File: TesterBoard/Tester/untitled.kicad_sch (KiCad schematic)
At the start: 37 parts, among them SW10 SW_Push, SW2 SW_Push, SW3 SW_Push, SW4 SW_Push, SW5 SW_Push, SW6 SW_Push, SW7 SW_Push, SW8 SW_Push, U10 74HC244, U3 74LS14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

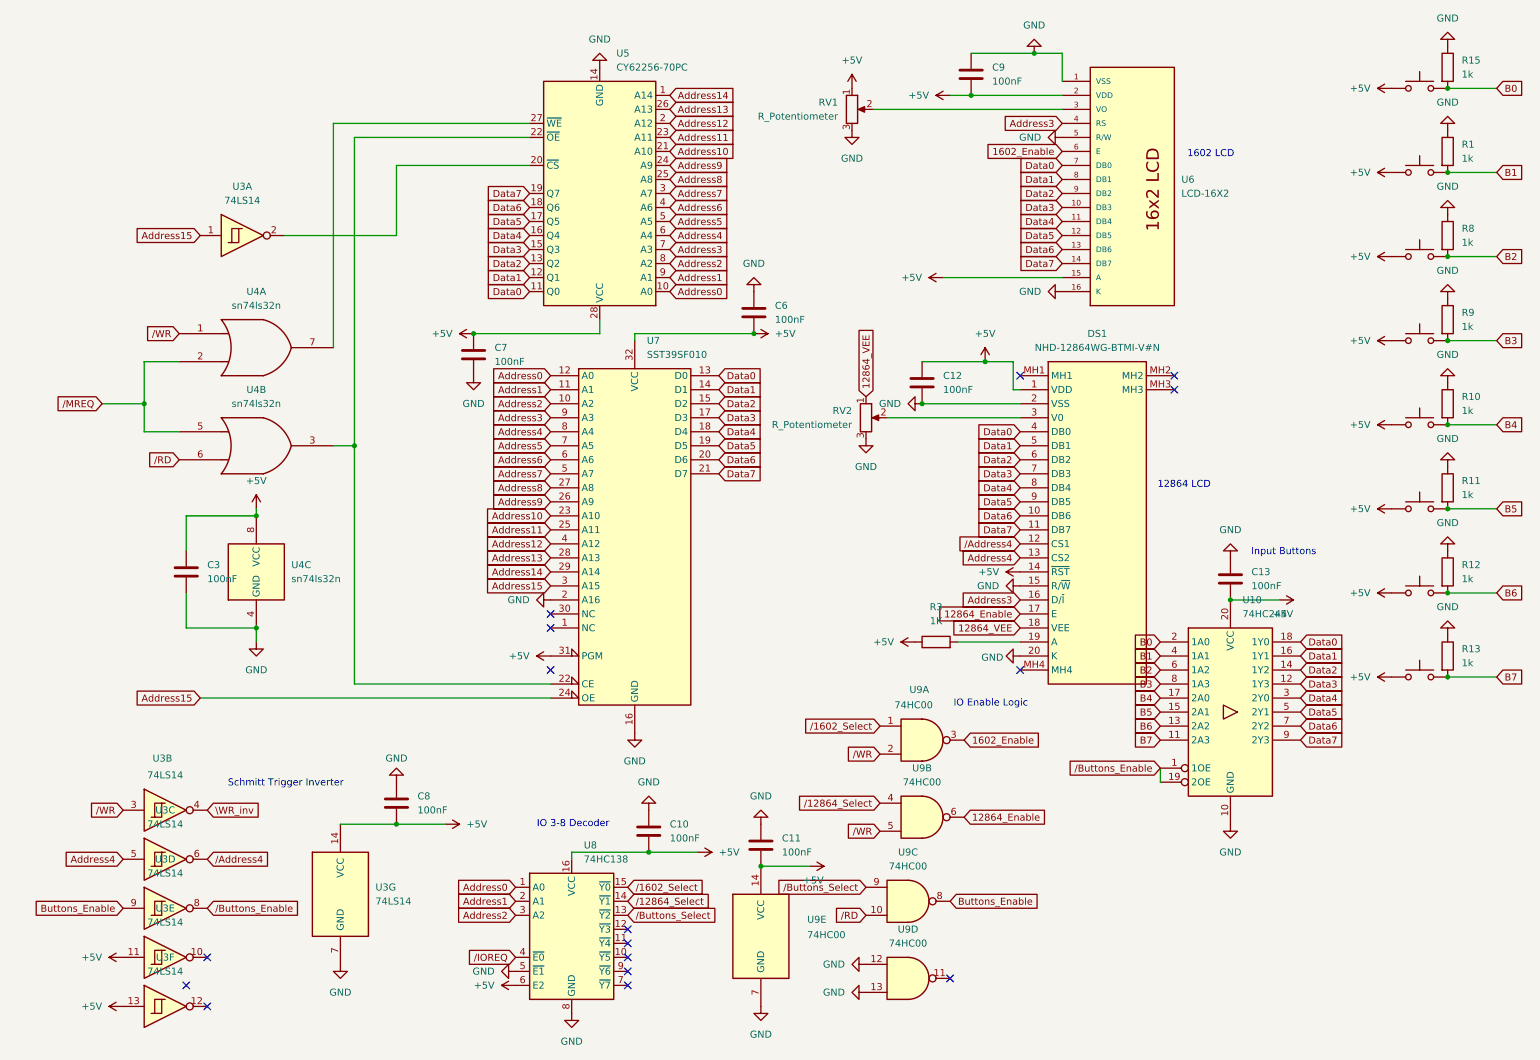
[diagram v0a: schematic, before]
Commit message: updated PCB to fix logic, ready to place and route
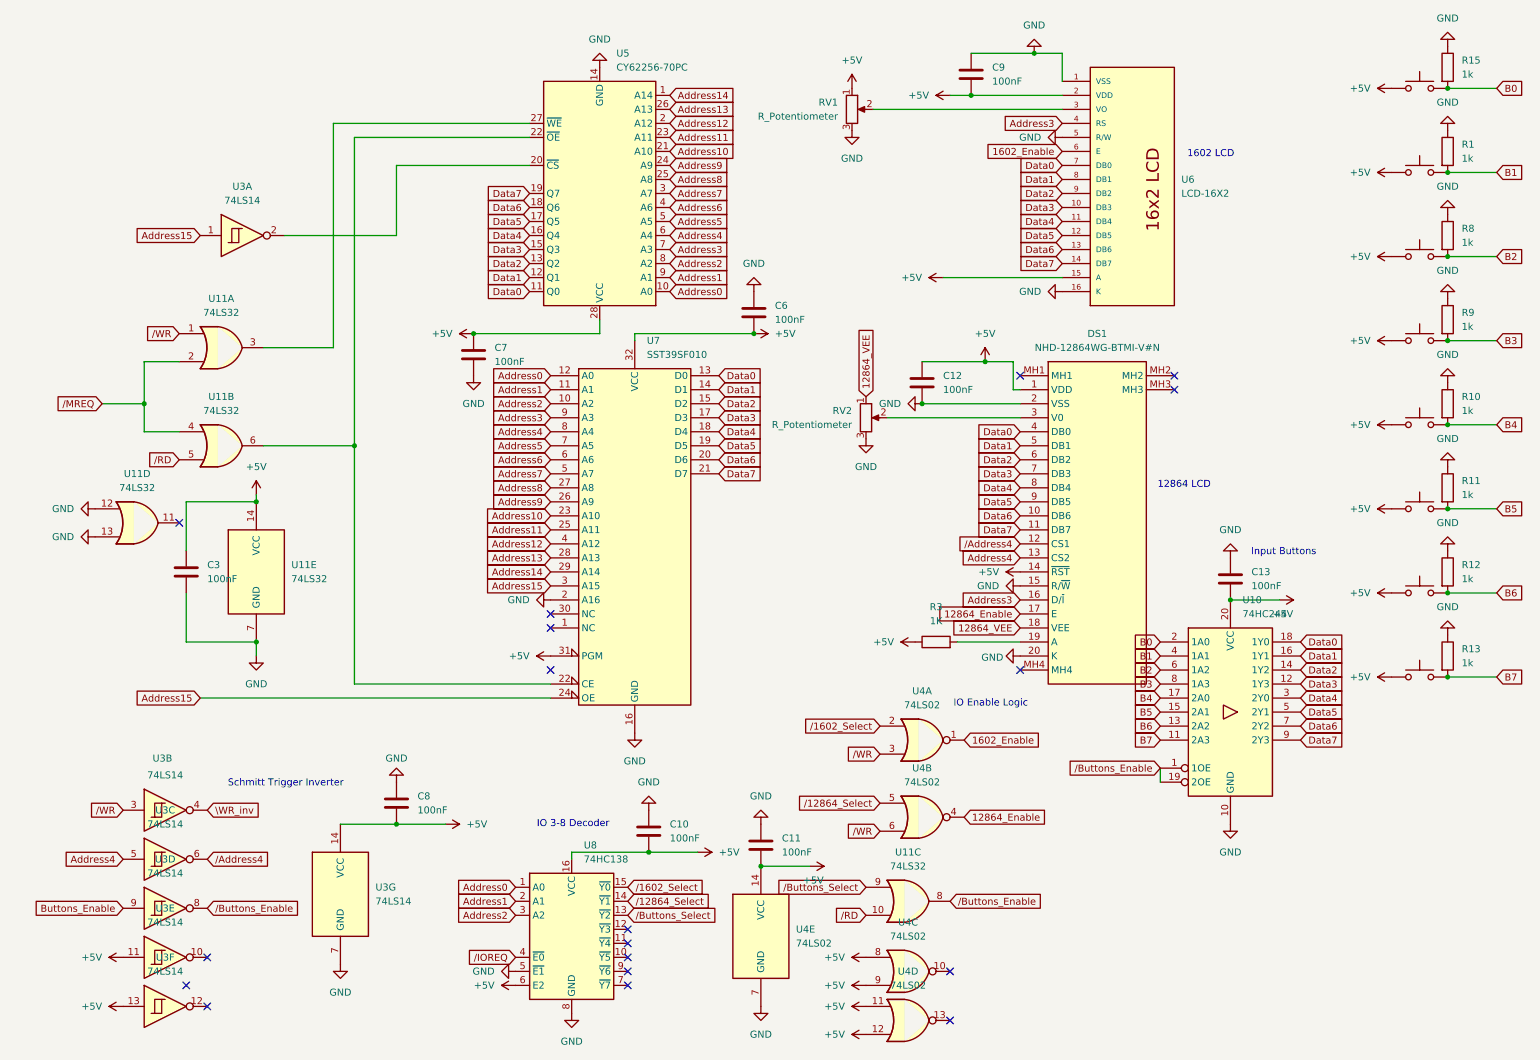
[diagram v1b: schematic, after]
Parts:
- removed U4: sn74ls32n, Package_DIP:DIP-14_W7.62mm_Socket, symbol 74xGxx:74AUC2G32
- removed U9: 74HC00, Package_DIP:DIP-14_W7.62mm_Socket, symbol 74xx:74HC00
- added U11: 74LS32, Package_DIP:DIP-14_W7.62mm_Socket, symbol 74xx:74LS32
- added U4: 74LS02, Package_DIP:DIP-14_W7.62mm_Socket, symbol 74xx:74LS02
- U5: footprint Package_DIP:DIP-28_W15.24mm -> Package_DIP:DIP-28_W15.24mm_Socket
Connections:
- net +5V: now also U11.14 (VCC), U4.11, U4.12, U4.14 (VCC), U4.8, U4.9
- net 12864_Enable: now also U4.4
- net 1602_Enable: now also U4.1
- net GND: now also U11.12, U11.13, U11.7 (GND), U4.7 (GND)
- net /12864_Select: now also U4.5
- net /1602_Select: now also U4.2
- net /Buttons_Enable: now also U11.8
- net /Buttons_Select: now also U11.9
- net /MREQ: now also U11.2, U11.4
- net /RD: now also U11.10, U11.5
- net /WR: now also U11.1, U4.3, U4.6
- net at U5.22 (~{OE}), U7.22 (CE): now also U11.6
- net at U5.27 (~{WE}): now also U11.3
- no-connect marks 16 -> 18

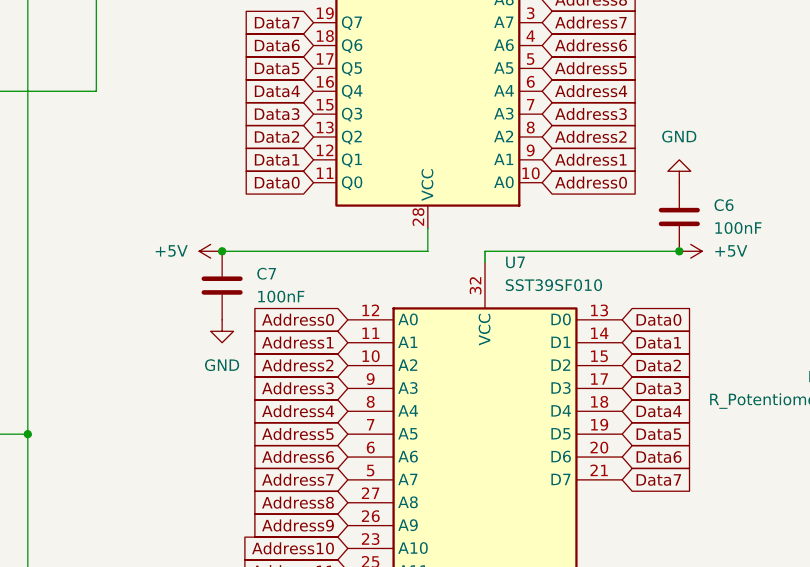
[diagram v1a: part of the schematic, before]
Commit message: minor changes to pcb : labels for schematic
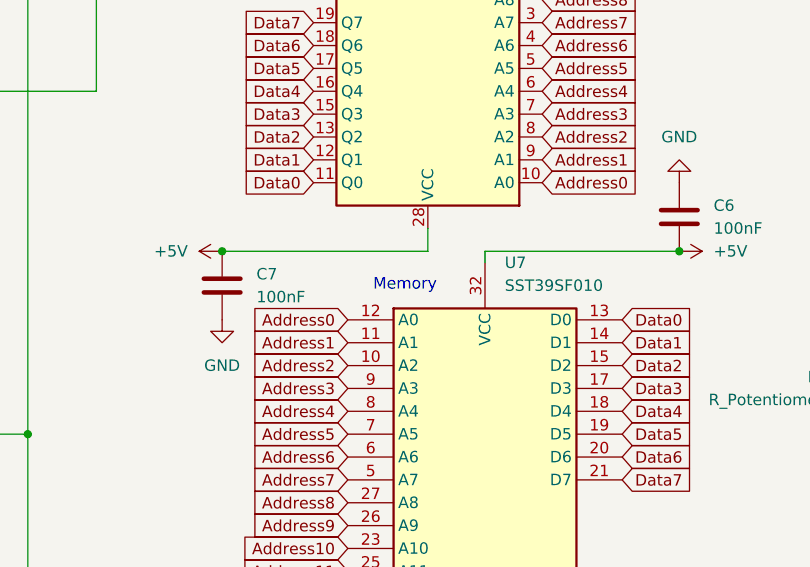
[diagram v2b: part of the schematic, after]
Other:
- note added: "Memory"
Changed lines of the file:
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@@
+		)
+	)
+	(text "Memory"
+		(exclude_from_sim no)
+		(at 109.22 72.39 0)
+		(effects
+			(font
+				(size 1.27 1.27)
+			)
 		)
 	)

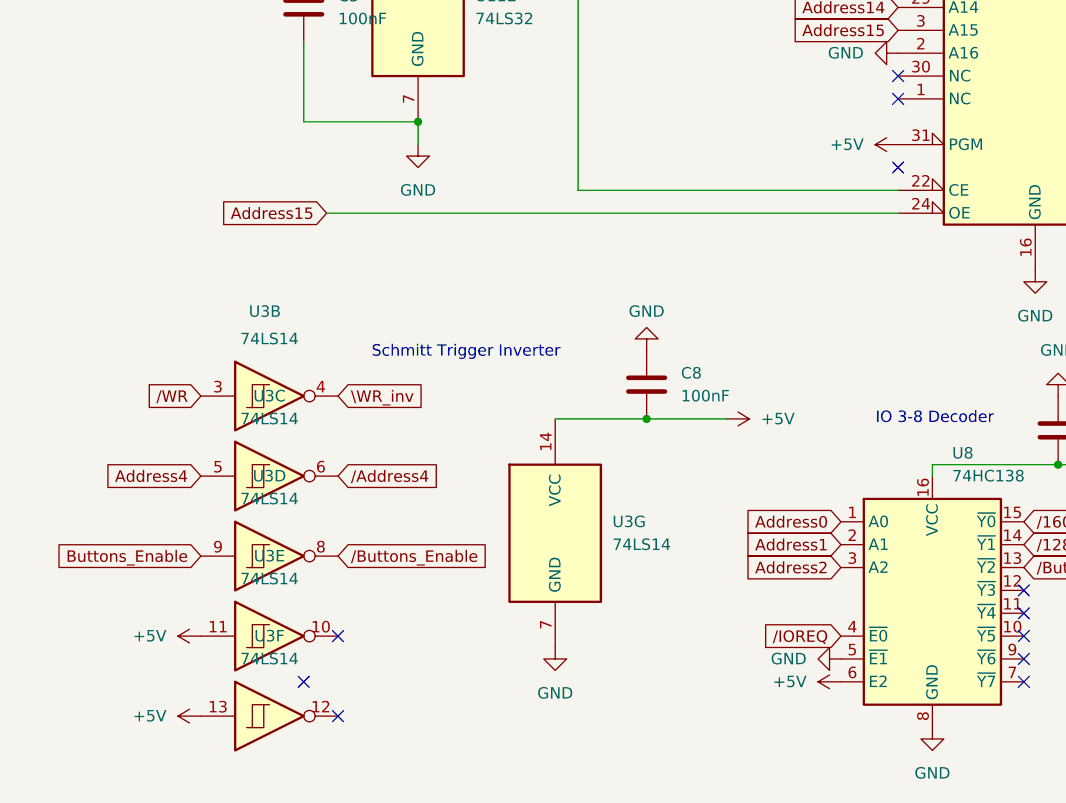
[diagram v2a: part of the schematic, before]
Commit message: Cleared errors on schematic - superfluous enable signal
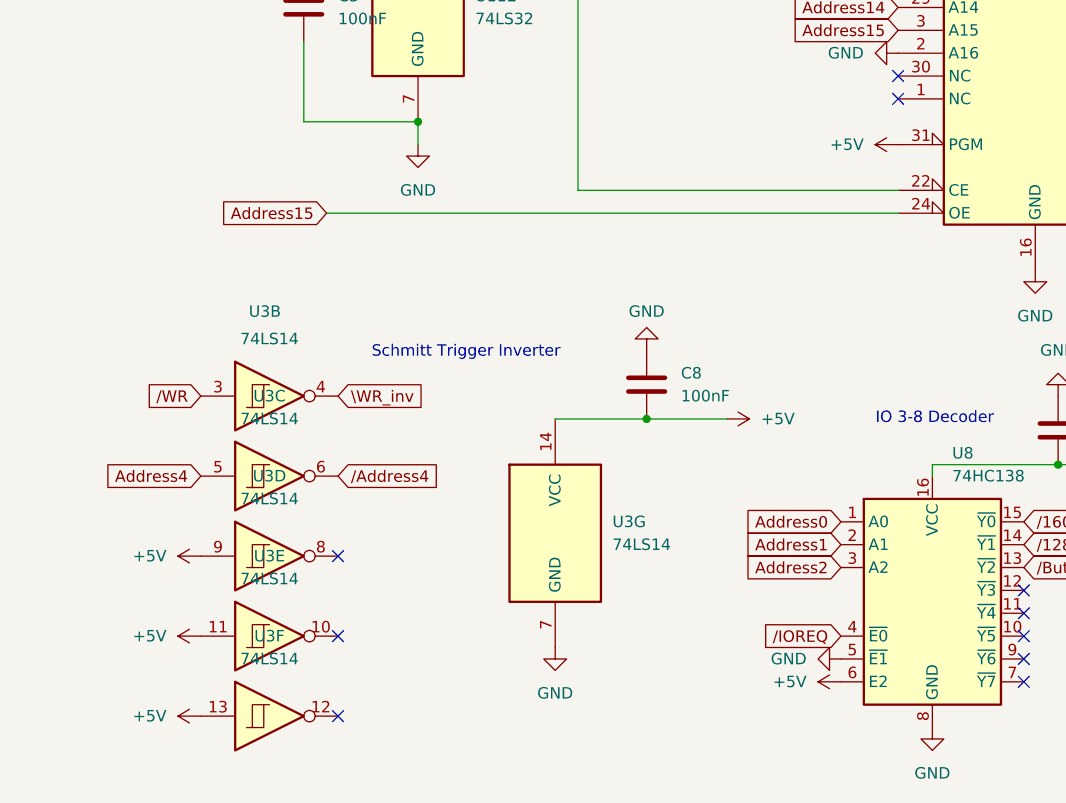
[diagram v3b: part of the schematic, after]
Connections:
- net Buttons_Enable is gone; now on net +5V: U3.9
- net /Buttons_Enable: no longer U3.8
- no-connect marks 18 -> 17
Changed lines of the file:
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@@
 	)
 	(no_connect
-		(at 36.83 186.69)
-	)
-	(no_connect
 		(at 102.87 121.92)
 	)
@@
 	)
 	(no_connect
-		(at 175.26 193.04)
+		(at 40.64 172.72)
 	)
 	(no_connect
-		(at 102.87 129.54)
+		(at 175.26 193.04)
 	)
 	(no_connect
@@
 		)
 	)
-	(global_label "Buttons_Enable"
-		(shape input)
-		(at 25.4 172.72 180)
-		(fields_autoplaced yes)
-		(effects
-			(font
-				(size 1.27 1.27)
-			)
-			(justify right)
-		)
-		(property "Intersheetrefs" "${INTERSHEET_REFS}"
-			(at 7.9009 172.72 0)
-			(effects
-				(font
-					(size 1.27 1.27)
-				)
-				(justify right)
-				(hide yes)
-			)
-		)
-	)
 	(global_label "Address8"
 		(shape input)
@@
 		)
 	)
-	(global_label "{slash}Buttons_Enable"
-		(shape input)
-		(at 40.64 172.72 0)
-		(fields_autoplaced yes)
-		(effects
-			(font
-				(size 1.27 1.27)
-			)
-			(justify left)
-		)
-		(property "Intersheetrefs" "${INTERSHEET_REFS}"
-			(at 59.4696 172.72 0)
-			(effects
-				(font
-					(size 1.27 1.27)
-				)
-				(justify left)
-				(hide yes)
-			)
-		)
-	)
 	(global_label "Address4"
 		(shape input)
@@
 					(unit 1)
 				)
+			)
+		)
+	)
+	(symbol
+		(lib_id "power:+5V")
+		(at 25.4 172.72 90)
+		(unit 1)
+		(exclude_from_sim no)
+		(in_bom yes)
+		(on_board yes)
+		(dnp no)
+		(fields_autoplaced yes)
+		(property "Reference" "#PWR079"
+			(at 29.21 172.72 0)
+			(effects
+				(font
+					(size 1.27 1.27)
+				)
+				(hide yes)
+			)
+		)
+		(property "Value" "+5V"
+			(at 21.59 172.7199 90)
+			(effects
+				(font
+					(size 1.27 1.27)
+				)
+				(justify left)
+			)
+		)
+		(property "Footprint" ""
+			(at 25.4 172.72 0)
+			(effects
+				(font
+					(size 1.27 1.27)
+				)
+				(hide yes)
+			)
+		)
+		(property "Datasheet" ""
+			(at 25.4 172.72 0)
+			(effects
+				(font
+					(size 1.27 1.27)
+				)
+				(hide yes)
+			)
+		)
+		(property "Description" "Power symbol creates a global label with name \"+5V\""
+			(at 25.4 172.72 0)
+			(effects
+				(font
+					(size 1.27 1.27)
+				)
+				(hide yes)
+			)
+		)
+		(pin "1"
+		)
+		(instances
+			(project "Tester"
+				(path "/806dc3e0-8575-4e5d-8446-51f379cb8ec6/3cbfe4a7-b38f-43f7-b38e-5a686bf242d5"
+					(reference "#PWR079")
+					(unit 1)
+				)

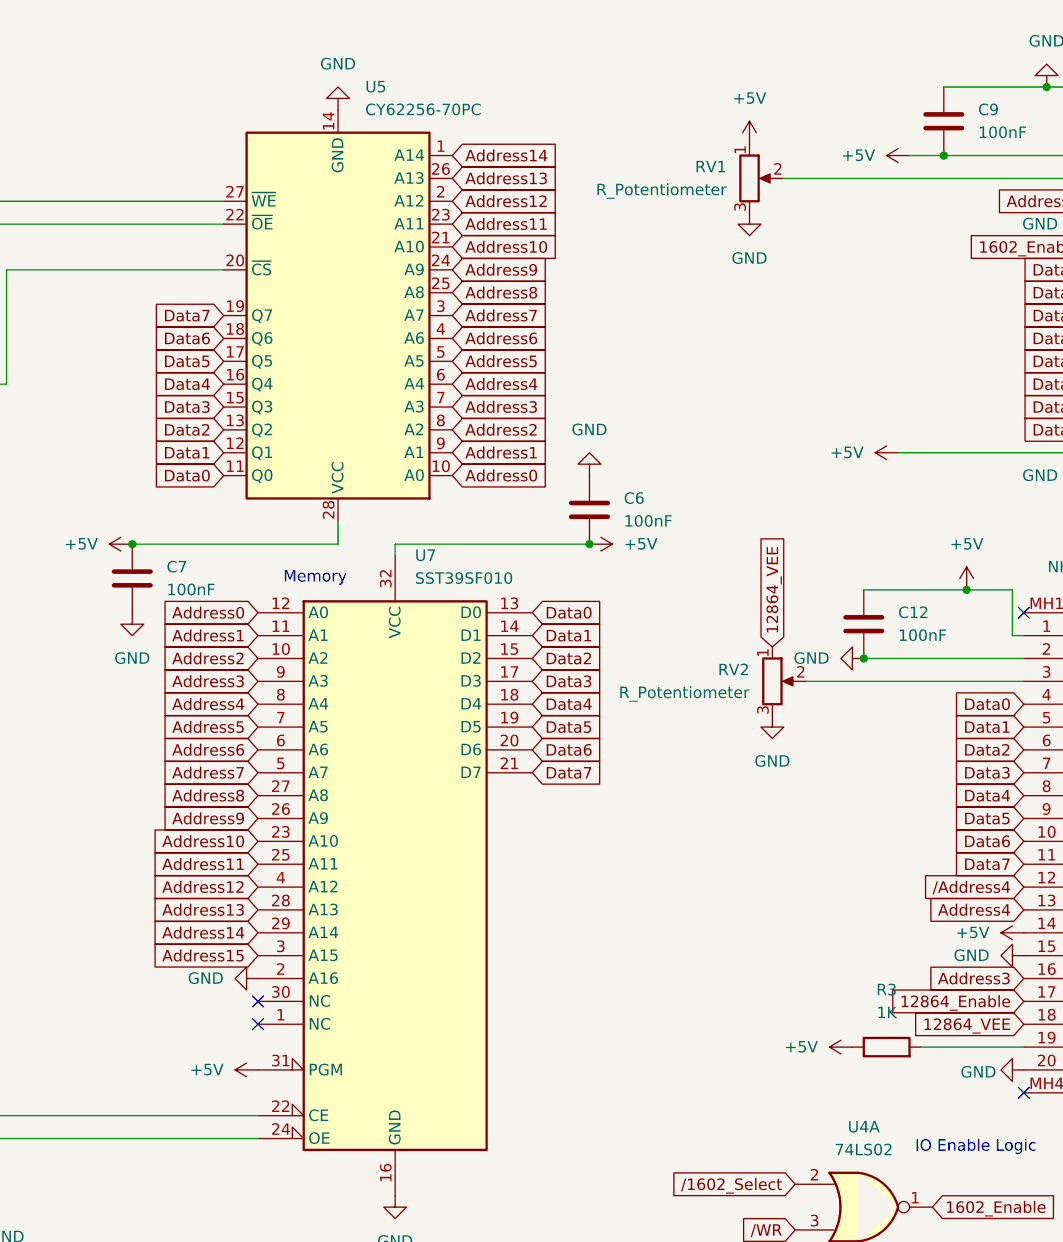
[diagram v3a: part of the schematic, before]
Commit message: Placed PCB awaiting review
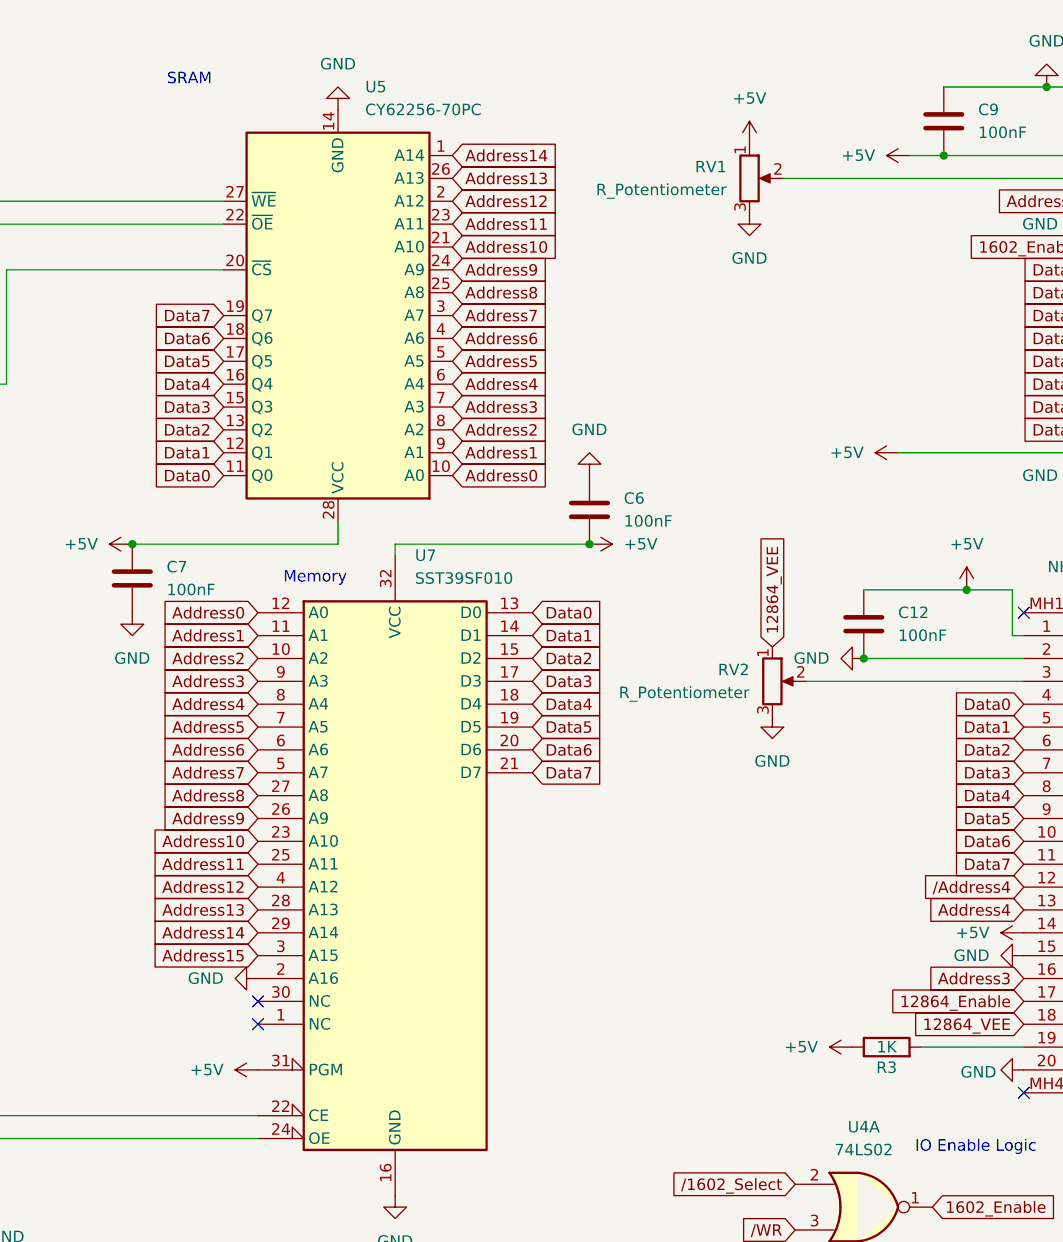
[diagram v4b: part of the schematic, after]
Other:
- note added: "SRAM"
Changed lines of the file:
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@@
 		)
 	)
+	(text "SRAM"
+		(exclude_from_sim no)
+		(at 95.25 17.018 0)
+		(effects
+			(font
+				(size 1.27 1.27)
+			)
+		)
+	)
 	(text "1602 LCD"
 		(exclude_from_sim no)
@@
 		(on_board yes)
 		(dnp no)
-		(fields_autoplaced yes)
 		(property "Reference" "R3"
-			(at 172.72 118.11 90)
+			(at 172.72 126.746 90)
 			(effects
 				(font
@@
 		)
 		(property "Value" "1K"
-			(at 172.72 120.65 90)
+			(at 172.72 124.46 90)
 			(effects
 				(font
